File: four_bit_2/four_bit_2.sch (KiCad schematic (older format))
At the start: 1 part, among them P1 DIN_41612_128P

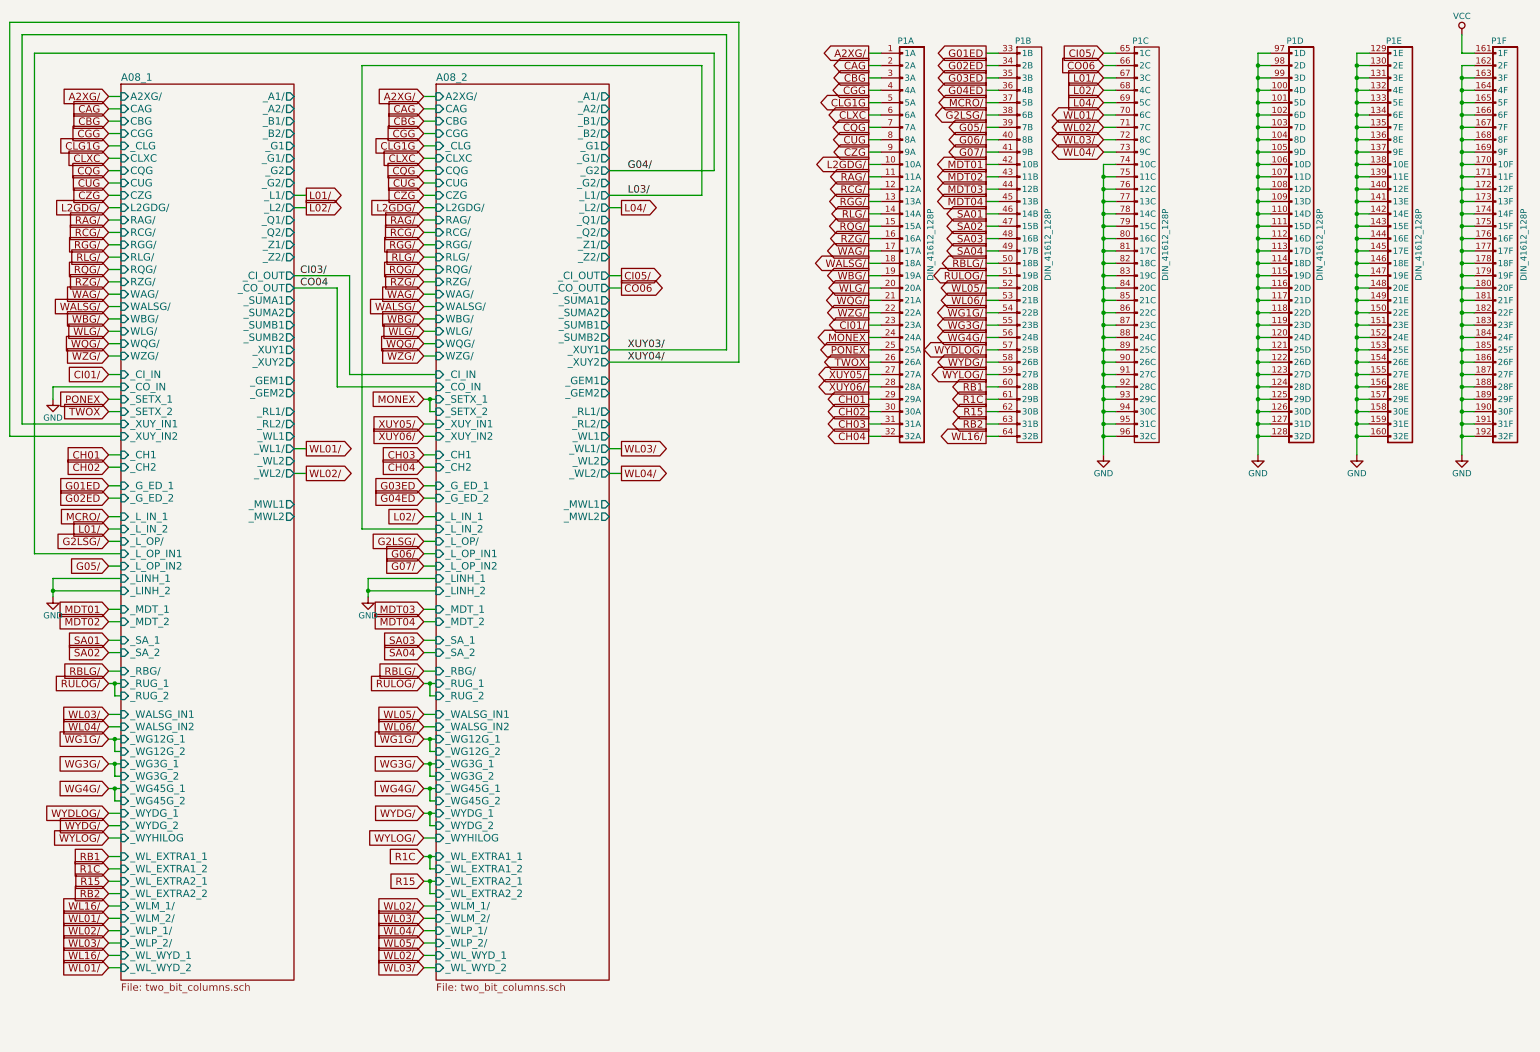
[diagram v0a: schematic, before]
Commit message: Fully added / tied in module 9. Yay for identical logic!
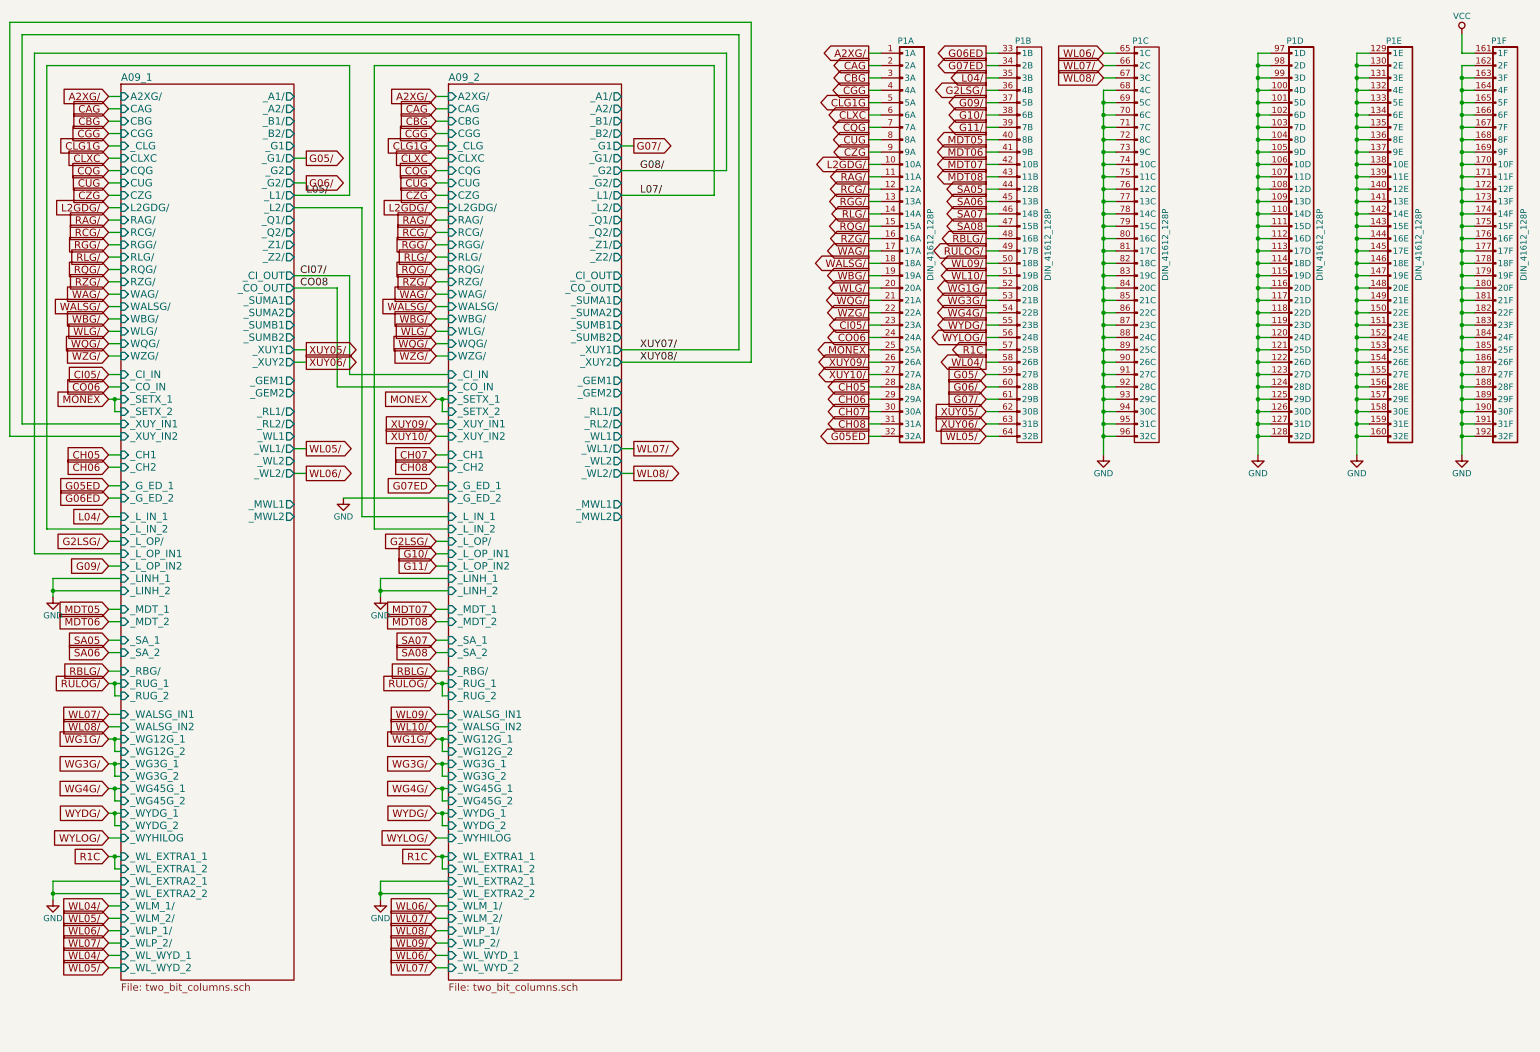
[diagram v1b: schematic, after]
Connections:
- net CI01/ is gone; now on net CI05/: P1.23 (23A)
- net G03ED is gone; now on net L04/: P1.35 (3B)
- net G04ED is gone; now on net G2LSG/: P1.36 (4B)
- net L02/ is gone; now on net GND: P1.68 (4C)
- net PONEX is gone; now on net MONEX: P1.25 (25A)
- net R15 is gone; now on net XUY05/: P1.62 (30B)
- net RB1 is gone; now on net G06/: P1.60 (28B)
- net RB2 is gone; now on net XUY06/: P1.63 (31B)
- net SA03 is gone; now on net RBLG/: P1.48 (16B)
- net SA04 is gone; now on net RULOG/: P1.49 (17B)
- net WL01/ is gone; now on net GND: P1.70 (6C)
- net WL02/ is gone; now on net GND: P1.71 (7C)
- net WL03/ is gone; now on net GND: P1.72 (8C)
- net WL16/ is gone; now on net WL05/: P1.64 (32B)
- net WYDLOG/ is gone; now on net R1C: P1.57 (25B)
- net CI05/: no longer P1.65 (1C)
- net CO06: now also P1.24 (24A); no longer P1.66 (2C)
- net G05/: now also P1.59 (27B); no longer P1.39 (7B)
- net G06/: no longer P1.40 (8B)
- net G07/: now also P1.61 (29B); no longer P1.41 (9B)
- net G2LSG/: no longer P1.38 (6B)
- net GND: now also P1.69 (5C), P1.73 (9C)
- net L04/: no longer P1.69 (5C)
- net MONEX: no longer P1.24 (24A)
- net R1C: no longer P1.61 (29B)
- net RBLG/: no longer P1.50 (18B)
- net RULOG/: no longer P1.51 (19B)
- net WG1G/: now also P1.52 (20B); no longer P1.54 (22B)
- net WG3G/: now also P1.53 (21B); no longer P1.55 (23B)
- net WG4G/: now also P1.54 (22B); no longer P1.56 (24B)
- net WL04/: now also P1.58 (26B); no longer P1.73 (9C)
- net WL05/: no longer P1.52 (20B)
- net WL06/: now also P1.65 (1C); no longer P1.53 (21B)
- net WYDG/: now also P1.55 (23B); no longer P1.58 (26B)
- net WYLOG/: now also P1.56 (24B); no longer P1.59 (27B)
- net XUY05/: no longer P1.27 (27A)
- net XUY06/: no longer P1.28 (28A)
- net CH01 renamed CH06
- net CH02 renamed CH07
- net CH03 renamed CH08
- net CH04 renamed G05ED
- net G01ED renamed G06ED
- net G02ED renamed G07ED
- net L01/ renamed WL08/
- net MCRO/ renamed G09/
- net MDT01 renamed MDT07
- net MDT02 renamed MDT08
- net MDT03 renamed SA05
- net MDT04 renamed SA06
- net SA01 renamed SA07
- net SA02 renamed SA08
- net TWOX renamed XUY09/
- new net CH05: P1.28 (28A)
- new net G10/: P1.38 (6B)
- new net G11/: P1.39 (7B)
- new net MDT05: P1.40 (8B)
- new net MDT06: P1.41 (9B)
- new net WL07/: P1.66 (2C)
- new net WL09/: P1.50 (18B)
- new net WL10/: P1.51 (19B)
- new net XUY10/: P1.27 (27A)

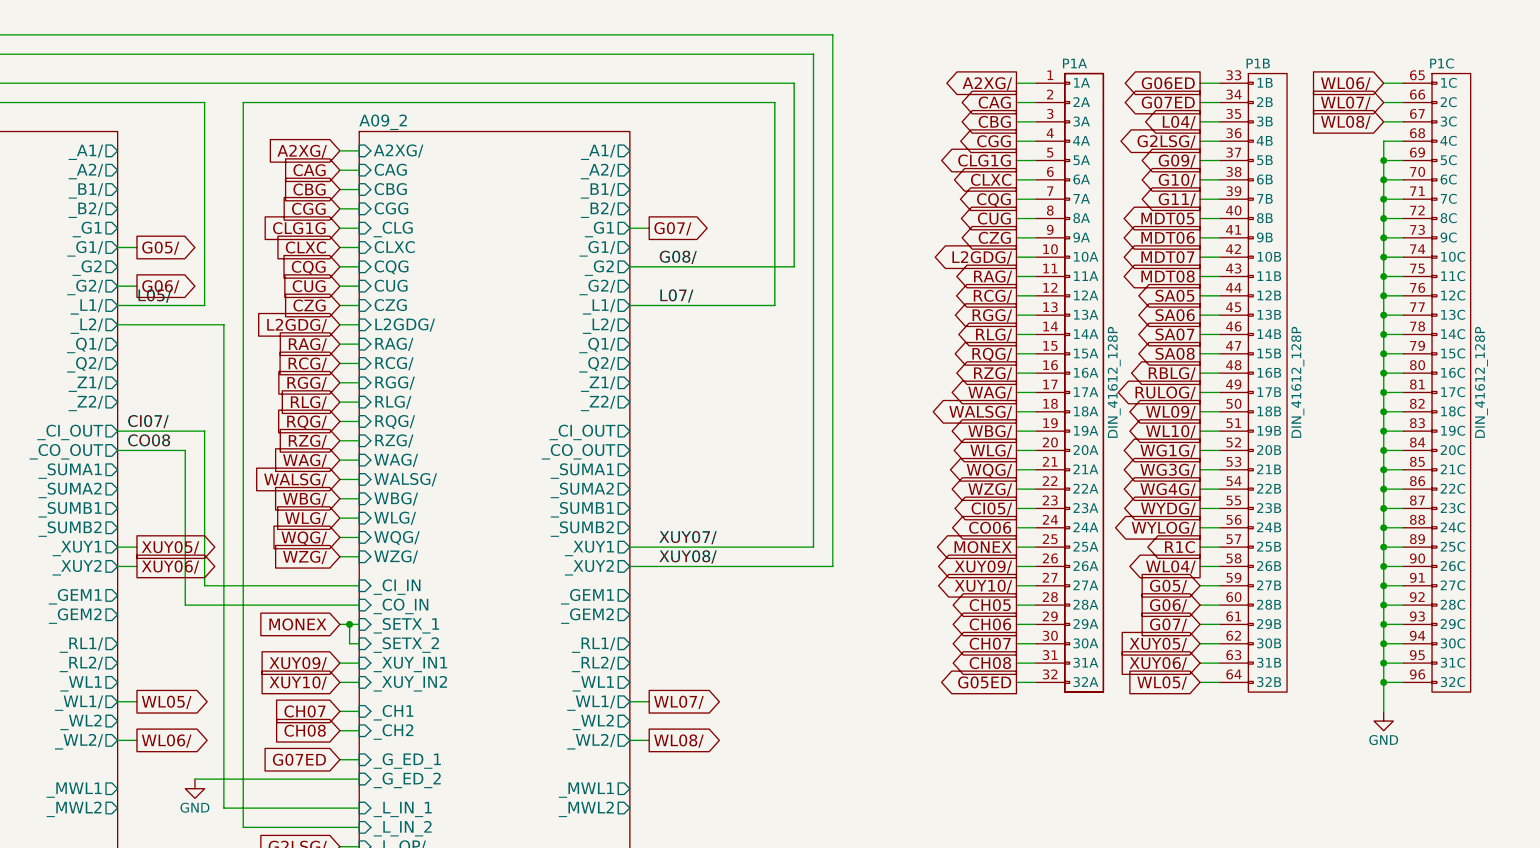
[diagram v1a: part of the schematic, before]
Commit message: Added a fully tied in module 10.
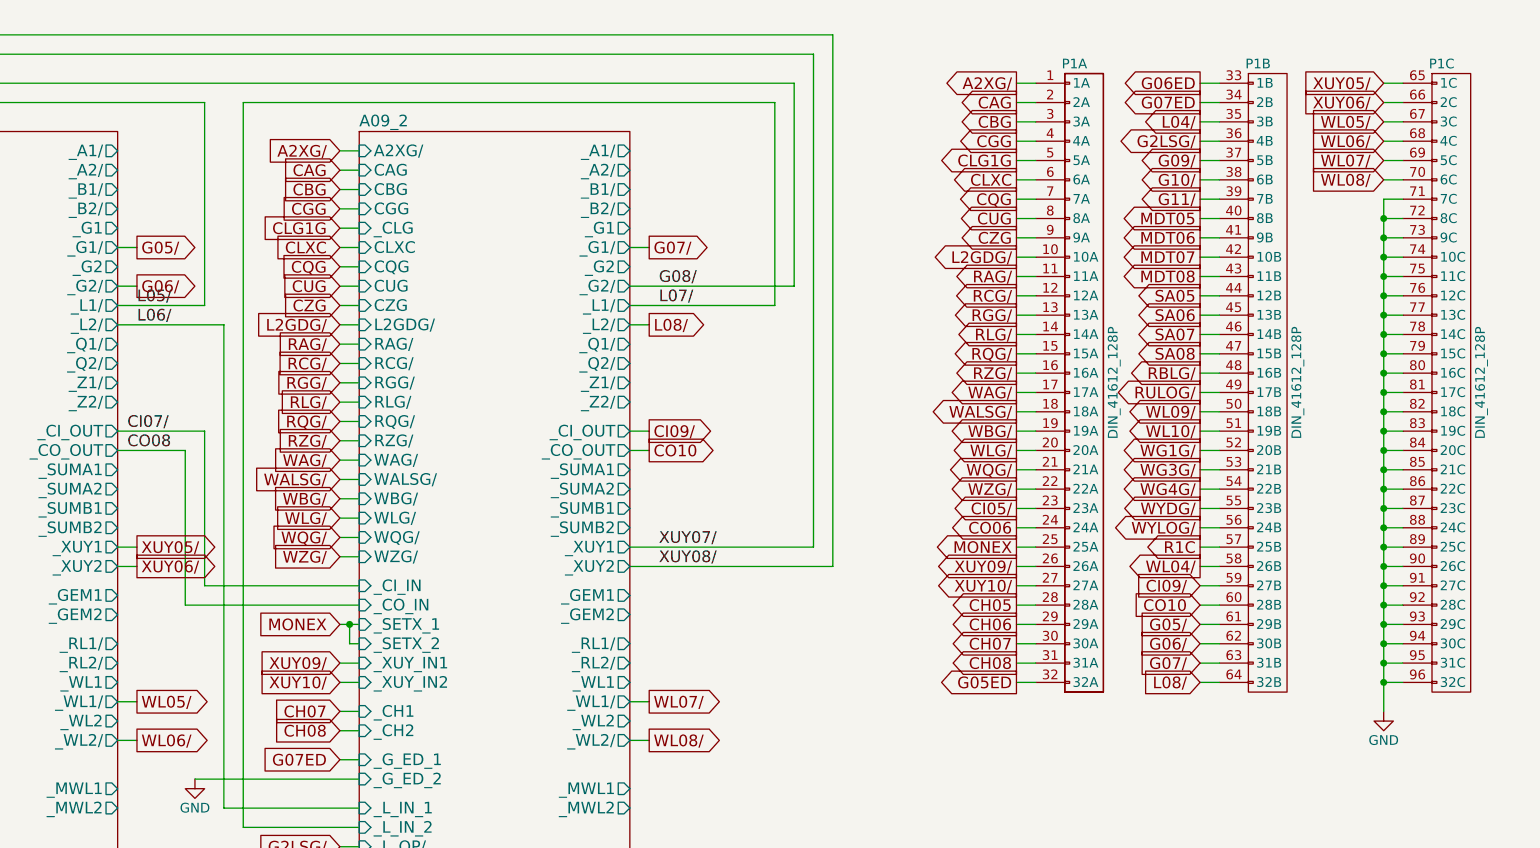
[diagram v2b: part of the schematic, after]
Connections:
- net G05/: now also P1.61 (29B); no longer P1.59 (27B)
- net G06/: now also P1.62 (30B); no longer P1.60 (28B)
- net G07/: now also P1.63 (31B); no longer P1.61 (29B)
- net GND: no longer P1.68 (4C), P1.69 (5C), P1.70 (6C)
- net WL05/: now also P1.67 (3C); no longer P1.64 (32B)
- net WL06/: now also P1.68 (4C); no longer P1.65 (1C)
- net WL07/: now also P1.69 (5C); no longer P1.66 (2C)
- net WL08/: now also P1.70 (6C); no longer P1.67 (3C)
- net XUY05/: now also P1.65 (1C); no longer P1.62 (30B)
- net XUY06/: now also P1.66 (2C); no longer P1.63 (31B)
- new net CI09/: P1.59 (27B)
- new net CO10: P1.60 (28B)
- new net L08/: P1.64 (32B)
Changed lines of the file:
@@
 	1    0    0    -1
 $EndComp
-Text Label 5950 1900 0    60   ~ 0
+Text Label 5950 2000 0    60   ~ 0
 G08/
 Text GLabel 1650 3650 0    60   Input ~ 0
@@
 Connection ~ 9700 4050
 Wire Wire Line
-	5800 1900 6650 1900
-Wire Wire Line
-	6650 1900 6650 950
+	5800 2000 6650 2000
+Wire Wire Line
+	6650 2000 6650 950
 Wire Wire Line
 	6650 950  1050 950
@@
 Wire Wire Line
 	3150 2000 3250 2000
-Text GLabel 5900 1700 2    60   Output ~ 0
+Text GLabel 5900 1800 2    60   Output ~ 0
 G07/
 Wire Wire Line
-	5800 1700 5900 1700
-Text GLabel 8750 3550 0    60   Input ~ 0
+	5800 1800 5900 1800
+Text GLabel 8750 3750 0    60   Input ~ 0
 G05/
-Text GLabel 8750 3650 0    60   Input ~ 0
+Text GLabel 8750 3850 0    60   Input ~ 0
 G06/
-Text GLabel 8750 3750 0    60   Input ~ 0
+Text GLabel 8750 3950 0    60   Input ~ 0
 G07/
 Wire Wire Line
-	8850 3550 8750 3550
-Wire Wire Line
-	8850 3650 8750 3650
-Wire Wire Line
 	8850 3750 8750 3750
 Wire Wire Line
-	9700 1450 9800 1450
-Connection ~ 9700 1450
-Connection ~ 9700 1550
-Wire Wire Line
-	9700 1250 9800 1250
-Wire Wire Line
-	9700 1350 9800 1350
-Connection ~ 9700 1350
-Wire Wire Line
-	9700 1250 9700 4200
+	8850 3850 8750 3850
+Wire Wire Line
+	8850 3950 8750 3950
+Wire Wire Line
+	9700 1550 9700 4200
 Text GLabel 3250 3350 2    60   Output ~ 0
 XUY05/
@@
 Wire Wire Line
 	3150 3450 3250 3450
-Text GLabel 8750 3850 0    60   Input ~ 0
+Text GLabel 9700 950  0    60   Input ~ 0
 XUY05/
-Text GLabel 8750 3950 0    60   Input ~ 0
+Text GLabel 9700 1050 0    60   Input ~ 0
 XUY06/
 Wire Wire Line
-	8850 3850 8750 3850
-Wire Wire Line
-	8850 3950 8750 3950
-Text GLabel 8750 4050 0    60   Input ~ 0
-WL05/
-Wire Wire Line
 	8850 4050 8750 4050
-Text GLabel 9700 950  0    60   Input ~ 0
-WL06/
-Wire Wire Line
-	9800 950  9700 950
-Text GLabel 9700 1050 0    60   Input ~ 0
-WL07/
 Wire Wire Line
 	9800 1050 9700 1050
 Text GLabel 9700 1150 0    60   Input ~ 0
+WL05/
+Wire Wire Line
+	9800 1150 9700 1150
+Text GLabel 9700 1250 0    60   Input ~ 0
+WL06/
+Wire Wire Line
+	9800 1250 9700 1250
+Text GLabel 9700 1350 0    60   Input ~ 0
+WL07/
+Wire Wire Line
+	9800 1350 9700 1350
+Text GLabel 9700 1450 0    60   Input ~ 0
 WL08/
 Wire Wire Line
-	9800 1150 9700 1150
+	9800 1450 9700 1450
+Text GLabel 5900 2750 2    60   Output ~ 0
+CI09/
+Wire Wire Line
+	5800 2750 5900 2750
+Text GLabel 5900 2850 2    60   Output ~ 0
+CO10
+Wire Wire Line
+	5800 2850 5900 2850
+Text GLabel 8750 3550 0    60   Input ~ 0
+CI09/
+Text GLabel 8750 3650 0    60   Input ~ 0
+CO10
+Wire Wire Line
+	8850 3550 8750 3550
+Wire Wire Line
+	8850 3650 8750 3650
+Text Label 3250 2200 0    60   ~ 0
+L06/
+Text GLabel 5900 2200 2    60   Output ~ 0
+L08/
+Wire Wire Line
+	5800 2200 5900 2200
+Wire Wire Line
+	9700 950  9800 950
+Text GLabel 8750 4050 0    60   Input ~ 0
+L08/
 $EndSCHEMATC
